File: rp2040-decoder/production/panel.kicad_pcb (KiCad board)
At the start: 4 copper layers, 70 x 70 mm, 511 parts, among them J4 5050662422, Q1 TPM2008, Q2 TPM2008, Q3 TPM2008, Q5 TPM2008, Q6 TPM2008, SW1 BOOT, U1 W25Q16JVUXIQ, U2 MT2492, U3 RP2040, U4 MD9927, U5 MAX98357A, Y1 X252012MMB4SI

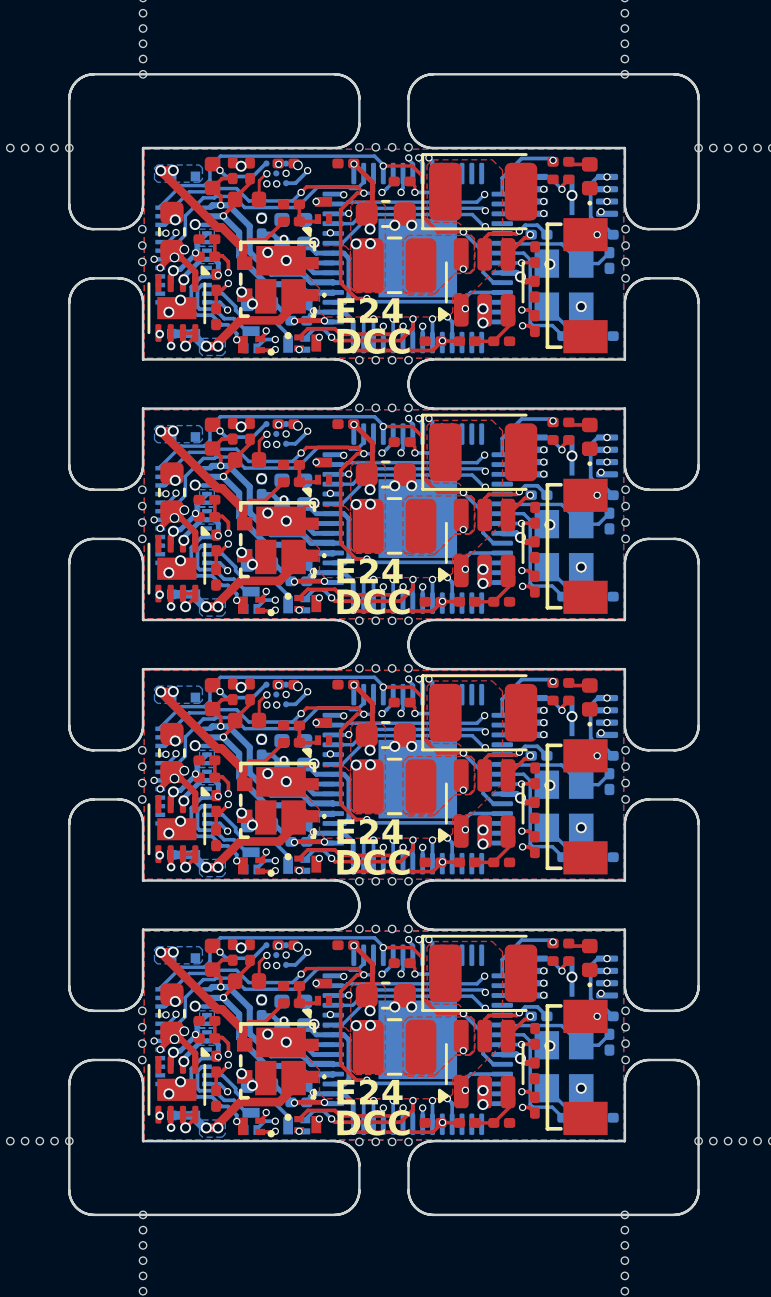
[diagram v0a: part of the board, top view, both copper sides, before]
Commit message: feat: upgrade flash to 8MB
feat: reorganize layout to be cleaner
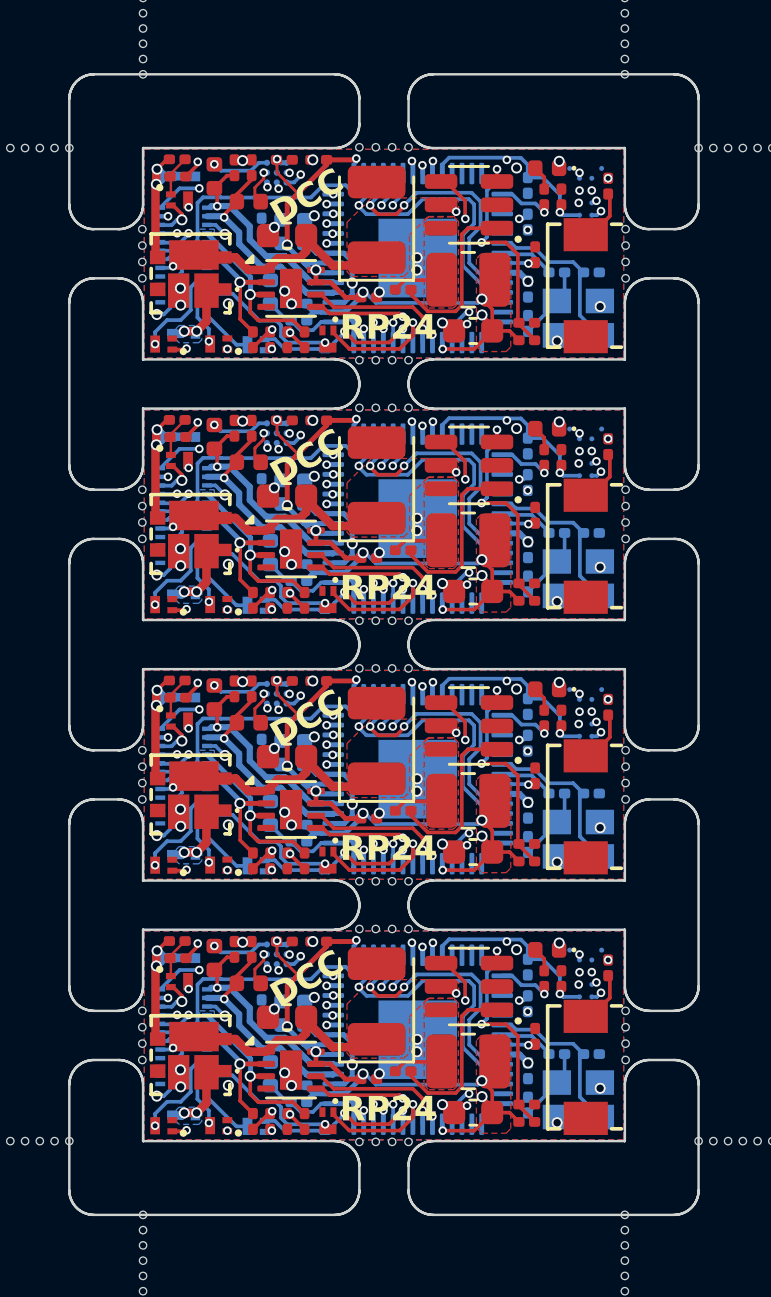
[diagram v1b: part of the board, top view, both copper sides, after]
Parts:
- removed the C1 at (157.7, 50.0)
- removed the C1 at (157.7, 60.6)
- removed the C1 at (157.7, 71.2)
- removed the C1 at (157.7, 39.4)
- removed the C14 at (143.4, 51.7)
- removed the C14 at (143.4, 72.9)
- removed the C14 at (143.4, 62.3)
- removed the C14 at (143.4, 41.1)
- removed the C16 at (146.9, 35.4)
- removed the C16 at (146.9, 46.0)
- removed the C16 at (146.9, 67.2)
- removed the C16 at (146.9, 56.6)
- removed the C17 at (149.2, 57.4)
- removed the C17 at (149.2, 36.2)
- removed the C17 at (149.2, 68.0)
- removed the C17 at (149.2, 46.8)
- removed the C18 at (139.9, 59.4)
- removed the C18 at (139.9, 70.0)
- removed the C18 at (139.9, 38.2)
- removed the C18 at (139.9, 48.8)
- removed the C19 at (150.5, 74.5)
- removed the C19 at (150.5, 53.3)
- removed the C19 at (150.5, 63.9)
- removed the C19 at (150.5, 42.7)
- removed the C2 at (155.7, 57.3)
- removed the C2 at (155.7, 36.1)
- removed the C2 at (155.7, 67.9)
- removed the C2 at (155.7, 46.7)
- removed the C20 at (143.1, 35.7)
- removed the C20 at (143.1, 46.3)
- removed the C20 at (143.1, 67.5)
- removed the C20 at (143.1, 56.9)
- removed the C21 at (144.5, 67.2)
- removed the C21 at (144.5, 35.4)
- removed the C21 at (144.5, 56.6)
- removed the C21 at (144.5, 46.0)
- removed the C22 at (142.3, 46.3)
- removed the C22 at (142.3, 56.9)
- removed the C22 at (142.3, 35.7)
- removed the C22 at (142.3, 67.5)
- removed the C3 at (157.5, 63.6)
- removed the C3 at (157.5, 42.5)
- removed the C3 at (157.5, 74.2)
- removed the C3 at (157.5, 53.0)
- removed the C4 at (152.5, 68.4)
- removed the C4 at (152.5, 57.8)
- removed the C4 at (152.5, 36.6)
- removed the C4 at (152.5, 47.2)
- removed the C6 at (154.6, 63.1)
- removed the C6 at (154.6, 73.7)
- removed the C6 at (154.6, 52.5)
- removed the C6 at (154.6, 41.9)
- removed the C7 at (154.6, 61.7)
- removed the C7 at (154.6, 72.3)
- removed the C7 at (154.6, 40.5)
- removed the C7 at (154.6, 51.1)
- removed the C9 at (148.6, 69.3)
- removed the C9 at (148.6, 37.5)
- removed the C9 at (148.6, 58.7)
- removed the C9 at (148.6, 48.1)
- removed the D1 at (144.2, 50.7)
- removed the D1 at (144.2, 71.9)
- removed the D1 at (144.2, 61.3)
- removed the D1 at (144.2, 40.1)
- removed the D2 at (156.9, 57.1)
- removed the D2 at (156.9, 35.9)
- removed the D2 at (156.9, 67.7)
- removed the D2 at (156.9, 46.5)
- removed the FB1 at (141.5, 46.5)
- removed the FB1 at (141.5, 35.9)
- removed the FB1 at (141.5, 67.7)
- removed the FB1 at (141.5, 57.1)
- removed the FB2 at (142.9, 58.1)
- removed the FB2 at (142.9, 47.5)
- removed the FB2 at (142.9, 68.7)
- removed the FB2 at (142.9, 36.9)
- removed the L1 at (148.9, 71.4)
- removed the L1 at (148.9, 39.6)
- removed the L1 at (148.9, 60.8)
- removed the L1 at (148.9, 50.2)
- removed the Q1 at (146.0, 37.3)
- removed the Q1 at (146.0, 69.1)
- removed the Q1 at (146.0, 58.5)
- removed the Q1 at (146.0, 47.9)
- removed the Q2 at (144.9, 64.0)
- removed the Q2 at (144.9, 53.4)
- removed the Q2 at (144.9, 42.8)
- removed the Q2 at (144.9, 74.6)
- removed the Q3 at (143.1, 42.8)
- removed the Q3 at (143.1, 74.6)
- removed the Q3 at (143.1, 53.4)
- removed the Q3 at (143.1, 64.0)
- removed the Q5 at (145.4, 42.7)
- removed the Q5 at (145.4, 74.5)
- removed the Q5 at (145.4, 53.3)
- removed the Q5 at (145.4, 63.9)
- removed the Q6 at (143.1, 63.8)
- removed the Q6 at (143.1, 74.4)
- removed the Q6 at (143.1, 53.2)
- removed the Q6 at (143.1, 42.6)
- removed the R1 at (144.7, 48.4)
- removed the R1 at (144.7, 59.0)
- removed the R1 at (144.7, 37.8)
- removed the R1 at (144.7, 69.6)
- removed the R10 at (145.0, 63.0)
- removed the R10 at (145.0, 52.4)
- removed the R10 at (145.0, 73.6)
- removed the R10 at (145.0, 41.8)
- removed the R11 at (141.7, 50.9)
- removed the R11 at (141.7, 72.1)
- removed the R11 at (141.7, 40.3)
- removed the R11 at (141.7, 61.5)
- removed the R12 at (141.7, 62.9)
- removed the R12 at (141.7, 41.7)
- removed the R12 at (141.7, 73.5)
- removed the R12 at (141.7, 52.3)
- removed the R13 at (141.3, 60.4)
- removed the R13 at (141.3, 39.2)
- removed the R13 at (141.3, 71.0)
- removed the R13 at (141.3, 49.8)
- removed the R14 at (141.3, 38.5)
- removed the R14 at (141.3, 49.1)
- removed the R14 at (141.3, 70.3)
- removed the R14 at (141.3, 59.7)
- removed the R2 at (144.7, 47.7)
- removed the R2 at (144.7, 58.3)
- removed the R2 at (144.7, 37.1)
- removed the R2 at (144.7, 68.9)
- removed the R4 at (157.5, 59.5)
- removed the R4 at (157.5, 70.1)
- removed the R4 at (157.5, 38.3)
- removed the R4 at (157.5, 48.9)
- removed the R5 at (154.8, 48.9)
- removed the R5 at (154.8, 38.3)
- removed the R5 at (154.8, 59.5)
- removed the R5 at (154.8, 70.1)
- removed the R6 at (156.1, 74.2)
- removed the R6 at (156.1, 63.6)
- removed the R6 at (156.1, 53.0)
- removed the R6 at (156.1, 42.5)
- removed the R7 at (153.3, 53.3)
- removed the R7 at (153.3, 63.9)
- removed the R7 at (153.3, 42.7)
- removed the R7 at (153.3, 74.5)
- removed the R8 at (151.9, 74.5)
- removed the R8 at (151.9, 42.7)
- removed the R8 at (151.9, 53.3)
- removed the R8 at (151.9, 63.9)
- removed the R9 at (155.7, 46.0)
- removed the R9 at (155.7, 35.4)
- removed the R9 at (155.7, 56.6)
- removed the R9 at (155.7, 67.2)
- removed the SW1 at (156.7, 72.2)
- removed the SW1 at (156.7, 61.6)
- removed the SW1 at (156.7, 51.0)
- removed the SW1 at (156.7, 40.4)
- removed the U1 at (156.2, 57.9)
- removed the U1 at (156.2, 47.3)
- removed the U1 at (156.2, 36.7)
- removed the U1 at (156.2, 68.5)
- removed the U2 at (152.6, 72.1)
- removed the U2 at (152.6, 40.3)
- removed the U2 at (152.6, 50.9)
- removed the U2 at (152.6, 61.5)
- removed the U4 at (140.1, 62.5)
- removed the U4 at (140.1, 51.9)
- removed the U4 at (140.1, 41.3)
- removed the U4 at (140.1, 73.1)
- removed the U5 at (144.1, 57.0)
- removed the U5 at (144.1, 67.6)
- removed the U5 at (144.1, 46.4)
- removed the U5 at (144.1, 35.8)
- removed the Y1 at (155.8, 61.6)
- removed the Y1 at (155.8, 51.0)
- removed the Y1 at (155.8, 72.2)
- removed the Y1 at (155.8, 40.4)
- added C1: 10pF, Capacitor_SMD:C_0201_0603Metric, B.Cu at (156.9, 71.7)
- added C1: 10pF, Capacitor_SMD:C_0201_0603Metric, B.Cu at (156.9, 50.5)
- added C1: 10pF, Capacitor_SMD:C_0201_0603Metric, B.Cu at (156.9, 61.1)
- added C1: 10pF, Capacitor_SMD:C_0201_0603Metric, B.Cu at (156.9, 39.9)
- added C14: 10uF, Capacitor_SMD:C_0402_1005Metric, B.Cu at (143.9, 61.9)
- added C14: 10uF, Capacitor_SMD:C_0402_1005Metric, B.Cu at (143.9, 51.3)
- added C14: 10uF, Capacitor_SMD:C_0402_1005Metric, B.Cu at (143.9, 72.5)
- added C14: 10uF, Capacitor_SMD:C_0402_1005Metric, B.Cu at (143.9, 40.7)
- added C16: 100nF, Capacitor_SMD:C_0201_0603Metric, F.Cu at (145.8, 35.3)
- added C16: 100nF, Capacitor_SMD:C_0201_0603Metric, F.Cu at (145.8, 67.1)
- added C16: 100nF, Capacitor_SMD:C_0201_0603Metric, F.Cu at (145.8, 45.9)
- added C16: 100nF, Capacitor_SMD:C_0201_0603Metric, F.Cu at (145.8, 56.5)
- added C17: 100nF, Capacitor_SMD:C_0201_0603Metric, B.Cu at (154.3, 68.1)
- added C17: 100nF, Capacitor_SMD:C_0201_0603Metric, B.Cu at (154.3, 57.5)
- added C17: 100nF, Capacitor_SMD:C_0201_0603Metric, B.Cu at (154.3, 36.3)
- added C17: 100nF, Capacitor_SMD:C_0201_0603Metric, B.Cu at (154.3, 46.9)
- added C18: 10uF, Capacitor_SMD:C_0603_1608Metric, F.Cu at (144.6, 70.2)
- added C18: 10uF, Capacitor_SMD:C_0603_1608Metric, F.Cu at (144.6, 38.4)
- added C18: 10uF, Capacitor_SMD:C_0603_1608Metric, F.Cu at (144.6, 59.6)
- added C18: 10uF, Capacitor_SMD:C_0603_1608Metric, F.Cu at (144.6, 49.0)
- added C19: 100nF, Capacitor_SMD:C_0201_0603Metric, F.Cu at (147.9, 40.9)
- added C19: 100nF, Capacitor_SMD:C_0201_0603Metric, F.Cu at (147.9, 72.7)
- added C19: 100nF, Capacitor_SMD:C_0201_0603Metric, F.Cu at (147.9, 51.5)
- added C19: 100nF, Capacitor_SMD:C_0201_0603Metric, F.Cu at (147.9, 62.1)
- added C2: 100nF, Capacitor_SMD:C_0201_0603Metric, F.Cu at (155.7, 47.4)
- added C2: 100nF, Capacitor_SMD:C_0201_0603Metric, F.Cu at (155.7, 68.6)
- added C2: 100nF, Capacitor_SMD:C_0201_0603Metric, F.Cu at (155.7, 36.8)
- added C2: 100nF, Capacitor_SMD:C_0201_0603Metric, F.Cu at (155.7, 58.0)
- added C20: 220pF, Capacitor_SMD:C_0201_0603Metric, F.Cu at (143.1, 35.6)
- added C20: 220pF, Capacitor_SMD:C_0201_0603Metric, F.Cu at (143.1, 56.8)
- added C20: 220pF, Capacitor_SMD:C_0201_0603Metric, F.Cu at (143.1, 46.2)
- added C20: 220pF, Capacitor_SMD:C_0201_0603Metric, F.Cu at (143.1, 67.4)
- added C21: 100nF, Capacitor_SMD:C_0201_0603Metric, F.Cu at (144.4, 45.9)
- added C21: 100nF, Capacitor_SMD:C_0201_0603Metric, F.Cu at (144.4, 67.1)
- added C21: 100nF, Capacitor_SMD:C_0201_0603Metric, F.Cu at (144.4, 56.5)
- added C21: 100nF, Capacitor_SMD:C_0201_0603Metric, F.Cu at (144.4, 35.3)
- added C22: 220pF, Capacitor_SMD:C_0201_0603Metric, F.Cu at (142.4, 67.4)
- added C22: 220pF, Capacitor_SMD:C_0201_0603Metric, F.Cu at (142.4, 56.8)
- added C22: 220pF, Capacitor_SMD:C_0201_0603Metric, F.Cu at (142.4, 35.6)
- added C22: 220pF, Capacitor_SMD:C_0201_0603Metric, F.Cu at (142.4, 46.2)
- added C3: 10pF, Capacitor_SMD:C_0201_0603Metric, B.Cu at (154.4, 73.7)
- added C3: 10pF, Capacitor_SMD:C_0201_0603Metric, B.Cu at (154.4, 41.9)
- added C3: 10pF, Capacitor_SMD:C_0201_0603Metric, B.Cu at (154.4, 63.1)
- added C3: 10pF, Capacitor_SMD:C_0201_0603Metric, B.Cu at (154.4, 52.5)
- added C4: 22uF, Capacitor_Tantalum_SMD:CP_EIA-3528-21_Kemet-B, F.Cu at (148.2, 69.5)
- added C4: 22uF, Capacitor_Tantalum_SMD:CP_EIA-3528-21_Kemet-B, F.Cu at (148.2, 37.7)
- added C4: 22uF, Capacitor_Tantalum_SMD:CP_EIA-3528-21_Kemet-B, F.Cu at (148.2, 48.3)
- added C4: 22uF, Capacitor_Tantalum_SMD:CP_EIA-3528-21_Kemet-B, F.Cu at (148.2, 58.9)
- added C6: 22nF, Capacitor_SMD:C_0201_0603Metric, F.Cu at (149.3, 72.4)
- added C6: 22nF, Capacitor_SMD:C_0201_0603Metric, F.Cu at (149.3, 40.6)
- added C6: 22nF, Capacitor_SMD:C_0201_0603Metric, F.Cu at (149.3, 51.2)
- added C6: 22nF, Capacitor_SMD:C_0201_0603Metric, F.Cu at (149.3, 61.8)
- added C7: 100nF, Capacitor_SMD:C_0201_0603Metric, B.Cu at (154.4, 40.5)
- added C7: 100nF, Capacitor_SMD:C_0201_0603Metric, B.Cu at (154.4, 51.1)
- added C7: 100nF, Capacitor_SMD:C_0201_0603Metric, B.Cu at (154.4, 61.7)
- added C7: 100nF, Capacitor_SMD:C_0201_0603Metric, B.Cu at (154.4, 72.3)
- added C9: 22uF, Capacitor_SMD:C_0603_1608Metric, F.Cu at (152.1, 42.2)
- added C9: 22uF, Capacitor_SMD:C_0603_1608Metric, F.Cu at (152.1, 52.8)
- added C9: 22uF, Capacitor_SMD:C_0603_1608Metric, F.Cu at (152.1, 74.0)
- added C9: 22uF, Capacitor_SMD:C_0603_1608Metric, F.Cu at (152.1, 63.4)
- added D1: NSR1030QMU, Local Library:NSR1030QMU, F.Cu at (140.6, 50.5)
- added D1: NSR1030QMU, Local Library:NSR1030QMU, F.Cu at (140.6, 71.7)
- added D1: NSR1030QMU, Local Library:NSR1030QMU, F.Cu at (140.6, 39.9)
- added D1: NSR1030QMU, Local Library:NSR1030QMU, F.Cu at (140.6, 61.1)
- added D2: Blue LED, LED_SMD:LED_0402_1005Metric, F.Cu at (155.1, 56.8)
- added D2: Blue LED, LED_SMD:LED_0402_1005Metric, F.Cu at (155.1, 46.2)
- added D2: Blue LED, LED_SMD:LED_0402_1005Metric, F.Cu at (155.1, 67.4)
- added D2: Blue LED, LED_SMD:LED_0402_1005Metric, F.Cu at (155.1, 35.6)
- added FB1: FB_P, Inductor_SMD:L_0402_1005Metric, F.Cu at (141.6, 36.0)
- added FB1: FB_P, Inductor_SMD:L_0402_1005Metric, F.Cu at (141.6, 57.1)
- added FB1: FB_P, Inductor_SMD:L_0402_1005Metric, F.Cu at (141.6, 67.8)
- added FB1: FB_P, Inductor_SMD:L_0402_1005Metric, F.Cu at (141.6, 46.5)
- added FB2: FB_N, Inductor_SMD:L_0402_1005Metric, F.Cu at (143.0, 68.8)
- added FB2: FB_N, Inductor_SMD:L_0402_1005Metric, F.Cu at (143.0, 58.2)
- added FB2: FB_N, Inductor_SMD:L_0402_1005Metric, F.Cu at (143.0, 37.0)
- added FB2: FB_N, Inductor_SMD:L_0402_1005Metric, F.Cu at (143.0, 47.6)
- added L1: 10uH, Inductor_SMD:L_1008_2520Metric, F.Cu at (151.9, 50.8)
- added L1: 10uH, Inductor_SMD:L_1008_2520Metric, F.Cu at (151.9, 40.2)
- added L1: 10uH, Inductor_SMD:L_1008_2520Metric, F.Cu at (151.9, 72.0)
- added L1: 10uH, Inductor_SMD:L_1008_2520Metric, F.Cu at (151.9, 61.4)
- added Q1: TPM2008, Local Library:Diodes_DFN1006-3, F.Cu at (140.2, 47.5)
- added Q1: TPM2008, Local Library:Diodes_DFN1006-3, F.Cu at (140.2, 58.1)
- added Q1: TPM2008, Local Library:Diodes_DFN1006-3, F.Cu at (140.2, 68.7)
- added Q1: TPM2008, Local Library:Diodes_DFN1006-3, F.Cu at (140.2, 36.9)
- added Q2: TPM2008, Local Library:Diodes_DFN1006-3, F.Cu at (146.2, 74.4)
- added Q2: TPM2008, Local Library:Diodes_DFN1006-3, F.Cu at (146.2, 42.6)
- added Q2: TPM2008, Local Library:Diodes_DFN1006-3, F.Cu at (146.2, 53.2)
- added Q2: TPM2008, Local Library:Diodes_DFN1006-3, F.Cu at (146.2, 63.8)
- added Q3: TPM2008, Local Library:Diodes_DFN1006-3, F.Cu at (139.5, 74.6)
- added Q3: TPM2008, Local Library:Diodes_DFN1006-3, F.Cu at (139.5, 42.8)
- added Q3: TPM2008, Local Library:Diodes_DFN1006-3, F.Cu at (139.5, 64.0)
- added Q3: TPM2008, Local Library:Diodes_DFN1006-3, F.Cu at (139.5, 53.4)
- added Q5: TPM2008, Local Library:Diodes_DFN1006-3, B.Cu at (143.3, 53.4)
- added Q5: TPM2008, Local Library:Diodes_DFN1006-3, B.Cu at (143.3, 74.6)
- added Q5: TPM2008, Local Library:Diodes_DFN1006-3, B.Cu at (143.3, 42.8)
- added Q5: TPM2008, Local Library:Diodes_DFN1006-3, B.Cu at (143.3, 64.0)
- added Q6: TPM2008, Local Library:Diodes_DFN1006-3, F.Cu at (141.8, 53.4)
- added Q6: TPM2008, Local Library:Diodes_DFN1006-3, F.Cu at (141.8, 74.6)
- added Q6: TPM2008, Local Library:Diodes_DFN1006-3, F.Cu at (141.8, 64.0)
- added Q6: TPM2008, Local Library:Diodes_DFN1006-3, F.Cu at (141.8, 42.8)
- added R1: 6.8k, Resistor_SMD:R_0201_0603Metric, F.Cu at (140.1, 45.9)
- added R1: 6.8k, Resistor_SMD:R_0201_0603Metric, F.Cu at (140.1, 67.1)
- added R1: 6.8k, Resistor_SMD:R_0201_0603Metric, F.Cu at (140.1, 56.5)
- added R1: 6.8k, Resistor_SMD:R_0201_0603Metric, F.Cu at (140.1, 35.3)
- added R10: 200R, Resistor_SMD:R_0201_0603Metric, B.Cu at (145.0, 52.4)
- added R10: 200R, Resistor_SMD:R_0201_0603Metric, B.Cu at (145.0, 41.8)
- added R10: 200R, Resistor_SMD:R_0201_0603Metric, B.Cu at (145.0, 63.0)
- added R10: 200R, Resistor_SMD:R_0201_0603Metric, B.Cu at (145.0, 73.6)
- added R11: 6.8k, Resistor_SMD:R_0201_0603Metric, F.Cu at (143.2, 42.6)
- added R11: 6.8k, Resistor_SMD:R_0201_0603Metric, F.Cu at (143.2, 53.2)
- added R11: 6.8k, Resistor_SMD:R_0201_0603Metric, F.Cu at (143.2, 74.4)
- added R11: 6.8k, Resistor_SMD:R_0201_0603Metric, F.Cu at (143.2, 63.8)
- added R12: 1k, Resistor_SMD:R_0201_0603Metric, F.Cu at (143.9, 53.2)
- added R12: 1k, Resistor_SMD:R_0201_0603Metric, F.Cu at (143.9, 42.6)
- added R12: 1k, Resistor_SMD:R_0201_0603Metric, F.Cu at (143.9, 74.4)
- added R12: 1k, Resistor_SMD:R_0201_0603Metric, F.Cu at (143.9, 63.8)
- added R13: 6.8k, Resistor_SMD:R_0201_0603Metric, F.Cu at (145.3, 53.2)
- added R13: 6.8k, Resistor_SMD:R_0201_0603Metric, F.Cu at (145.3, 74.4)
- added R13: 6.8k, Resistor_SMD:R_0201_0603Metric, F.Cu at (145.3, 42.6)
- added R13: 6.8k, Resistor_SMD:R_0201_0603Metric, F.Cu at (145.3, 63.8)
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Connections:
- U3 pad 51: Board_2-Net-(U1-IO3) -> Board_2-Net-(U1-IO2)
- U3 pad 52: Board_2-Net-(U1-CLK) -> Board_2-Net-(U1-IO3)
- U3 pad 53: Board_2-Net-(U1-DI(IO0)) -> Board_2-Net-(U1-CLK)
- U3 pad 54: Board_2-Net-(U1-IO2) -> Board_2-Net-(U1-DO(IO1))
- U3 pad 55: Board_2-Net-(U1-DO(IO1)) -> Board_2-Net-(U1-DI(IO0))
- U3 pad 51: Board_3-Net-(U1-IO3) -> Board_3-Net-(U1-IO2)
- U3 pad 52: Board_3-Net-(U1-CLK) -> Board_3-Net-(U1-IO3)
- U3 pad 53: Board_3-Net-(U1-DI(IO0)) -> Board_3-Net-(U1-CLK)
- U3 pad 54: Board_3-Net-(U1-IO2) -> Board_3-Net-(U1-DO(IO1))
- U3 pad 55: Board_3-Net-(U1-DO(IO1)) -> Board_3-Net-(U1-DI(IO0))
- U3 pad 51: Board_1-Net-(U1-IO3) -> Board_1-Net-(U1-IO2)
- U3 pad 52: Board_1-Net-(U1-CLK) -> Board_1-Net-(U1-IO3)
- U3 pad 53: Board_1-Net-(U1-DI(IO0)) -> Board_1-Net-(U1-CLK)
- U3 pad 54: Board_1-Net-(U1-IO2) -> Board_1-Net-(U1-DO(IO1))
- U3 pad 55: Board_1-Net-(U1-DO(IO1)) -> Board_1-Net-(U1-DI(IO0))
- U3 pad 51: Board_0-Net-(U1-IO3) -> Board_0-Net-(U1-IO2)
- U3 pad 52: Board_0-Net-(U1-CLK) -> Board_0-Net-(U1-IO3)
- U3 pad 53: Board_0-Net-(U1-DI(IO0)) -> Board_0-Net-(U1-CLK)
- U3 pad 54: Board_0-Net-(U1-IO2) -> Board_0-Net-(U1-DO(IO1))
- U3 pad 55: Board_0-Net-(U1-DO(IO1)) -> Board_0-Net-(U1-DI(IO0))
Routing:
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- removed copper zone on B.Cu, net Board_0-/TRACK_LEFT
- removed copper zone on In2.Cu, net Board_0-VDC
- removed copper zone on B.Cu, net Board_1-/TRACK_LEFT
- removed copper zone on In2.Cu, net Board_1-VDC
- removed copper zone on B.Cu, net Board_2-/TRACK_LEFT
- removed copper zone on In2.Cu, net Board_2-VDC
- removed copper zone on B.Cu, net Board_3-/TRACK_LEFT
- removed copper zone on In2.Cu, net Board_3-VDC
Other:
- board text added: "RP24"
- board text removed: "E24"

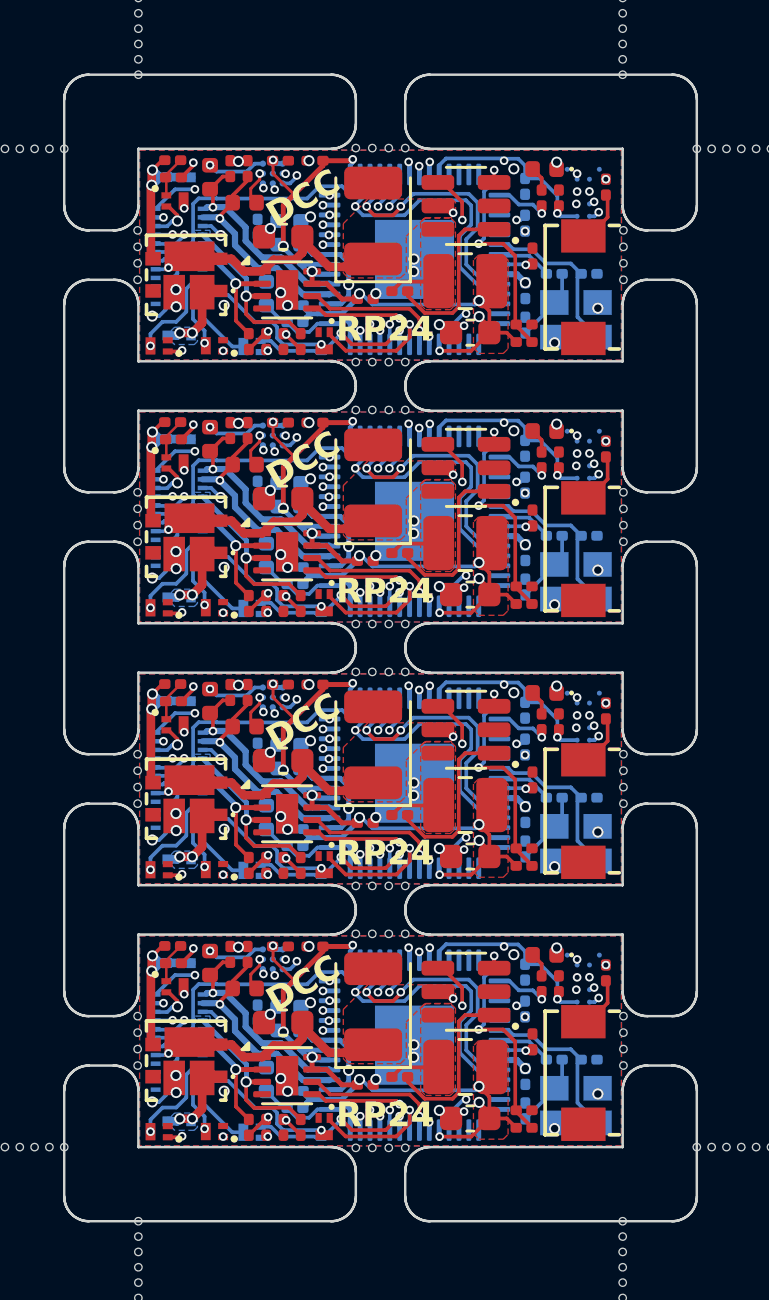
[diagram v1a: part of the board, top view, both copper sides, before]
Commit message: feat: add external capacitor support
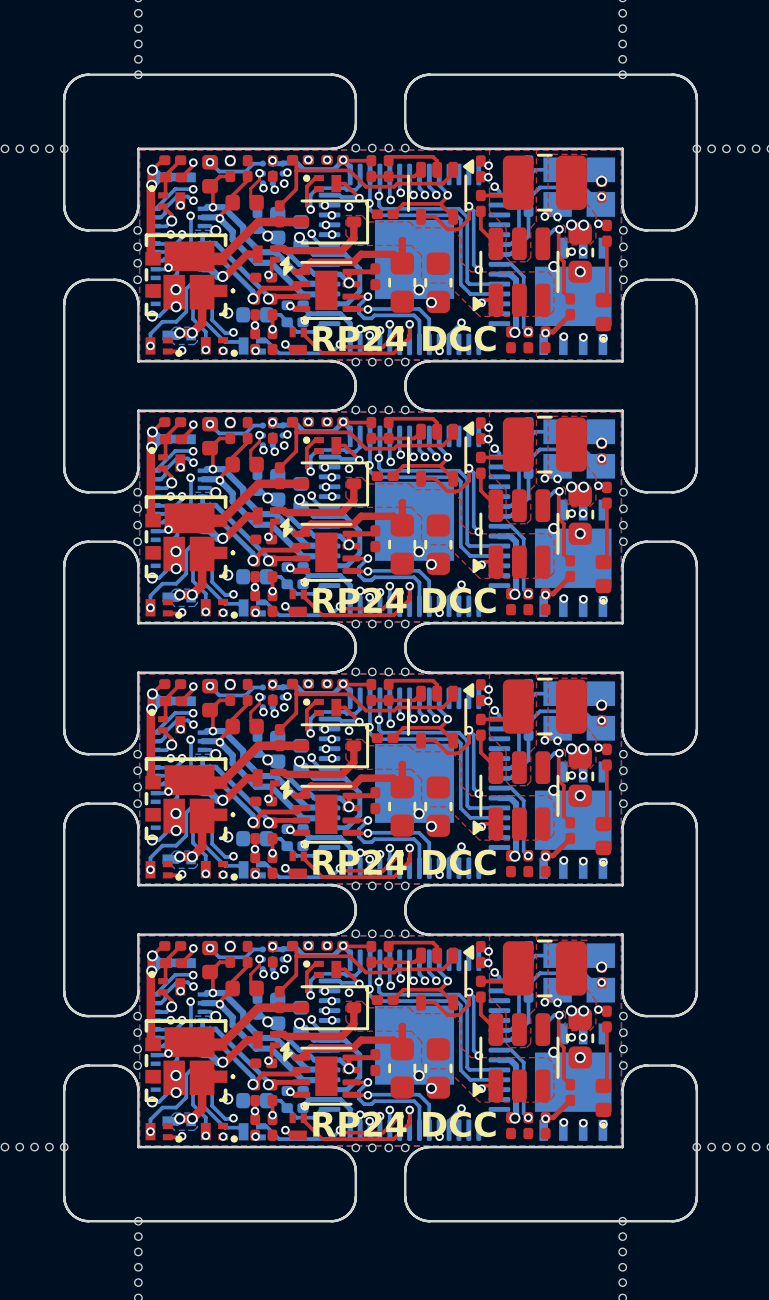
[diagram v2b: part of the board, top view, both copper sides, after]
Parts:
- removed the C1 at (156.9, 71.7)
- removed the C1 at (156.9, 50.5)
- removed the C1 at (156.9, 61.1)
- removed the C1 at (156.9, 39.9)
- removed the C10 at (144.3, 59.4)
- removed the C10 at (144.3, 38.2)
- removed the C10 at (144.3, 70.0)
- removed the C10 at (144.3, 48.8)
- removed the C12 at (143.5, 69.8)
- removed the C12 at (143.5, 59.2)
- removed the C12 at (143.5, 38.0)
- removed the C12 at (143.5, 48.6)
- removed the C13 at (154.7, 49.7)
- removed the C13 at (154.7, 39.1)
- removed the C13 at (154.7, 70.9)
- removed the C13 at (154.7, 60.3)
- removed the C14 at (143.9, 61.9)
- removed the C14 at (143.9, 51.3)
- removed the C14 at (143.9, 72.5)
- removed the C14 at (143.9, 40.7)
- removed the C16 at (145.8, 35.3)
- removed the C16 at (145.8, 67.1)
- removed the C16 at (145.8, 45.9)
- removed the C16 at (145.8, 56.5)
- removed the C17 at (154.3, 68.1)
- removed the C17 at (154.3, 57.5)
- removed the C17 at (154.3, 36.3)
- removed the C17 at (154.3, 46.9)
- removed the C18 at (144.6, 70.2)
- removed the C18 at (144.6, 38.4)
- removed the C18 at (144.6, 59.6)
- removed the C18 at (144.6, 49.0)
- removed the C19 at (147.9, 40.9)
- removed the C19 at (147.9, 72.7)
- removed the C19 at (147.9, 51.5)
- removed the C19 at (147.9, 62.1)
- removed the C2 at (155.7, 47.4)
- removed the C2 at (155.7, 68.6)
- removed the C2 at (155.7, 36.8)
- removed the C2 at (155.7, 58.0)
- removed the C21 at (144.4, 45.9)
- removed the C21 at (144.4, 67.1)
- removed the C21 at (144.4, 56.5)
- removed the C21 at (144.4, 35.3)
- removed the C3 at (154.4, 73.7)
- removed the C3 at (154.4, 41.9)
- removed the C3 at (154.4, 63.1)
- removed the C3 at (154.4, 52.5)
- removed the C4 at (148.2, 69.5)
- removed the C4 at (148.2, 37.7)
- removed the C4 at (148.2, 48.3)
- removed the C4 at (148.2, 58.9)
- removed the C6 at (149.3, 72.4)
- removed the C6 at (149.3, 40.6)
- removed the C6 at (149.3, 51.2)
- removed the C6 at (149.3, 61.8)
- removed the C7 at (154.4, 40.5)
- removed the C7 at (154.4, 51.1)
- removed the C7 at (154.4, 61.7)
- removed the C7 at (154.4, 72.3)
- removed the C8 at (145.3, 38.2)
- removed the C8 at (145.3, 59.4)
- removed the C8 at (145.3, 48.8)
- removed the C8 at (145.3, 70.0)
- removed the C9 at (152.1, 42.2)
- removed the C9 at (152.1, 52.8)
- removed the C9 at (152.1, 74.0)
- removed the C9 at (152.1, 63.4)
- removed the D2 at (155.1, 56.8)
- removed the D2 at (155.1, 46.2)
- removed the D2 at (155.1, 67.4)
- removed the D2 at (155.1, 35.6)
- removed the FB1 at (141.6, 36.0)
- removed the FB1 at (141.6, 57.1)
- removed the FB1 at (141.6, 67.8)
- removed the FB1 at (141.6, 46.5)
- removed the L1 at (151.9, 50.8)
- removed the L1 at (151.9, 40.2)
- removed the L1 at (151.9, 72.0)
- removed the L1 at (151.9, 61.4)
- removed the Q1 at (140.2, 47.5)
- removed the Q1 at (140.2, 58.1)
- removed the Q1 at (140.2, 68.7)
- removed the Q1 at (140.2, 36.9)
- removed the Q2 at (146.2, 74.4)
- removed the Q2 at (146.2, 42.6)
- removed the Q2 at (146.2, 53.2)
- removed the Q2 at (146.2, 63.8)
- removed the Q5 at (143.3, 53.4)
- removed the Q5 at (143.3, 74.6)
- removed the Q5 at (143.3, 42.8)
- removed the Q5 at (143.3, 64.0)
- removed the R11 at (143.2, 42.6)
- removed the R11 at (143.2, 53.2)
- removed the R11 at (143.2, 74.4)
- removed the R11 at (143.2, 63.8)
- removed the R12 at (143.9, 53.2)
- removed the R12 at (143.9, 42.6)
- removed the R12 at (143.9, 74.4)
- removed the R12 at (143.9, 63.8)
- removed the R13 at (145.3, 53.2)
- removed the R13 at (145.3, 74.4)
- removed the R13 at (145.3, 42.6)
- removed the R13 at (145.3, 63.8)
- removed the R14 at (144.6, 74.4)
- removed the R14 at (144.6, 42.6)
- removed the R14 at (144.6, 63.8)
- removed the R14 at (144.6, 53.2)
- removed the R4 at (157.6, 36.4)
- removed the R4 at (157.6, 57.5)
- removed the R4 at (157.6, 68.2)
- removed the R4 at (157.6, 47.0)
- removed R5 (x4): 100k, Resistor_SMD:R_0201_0603Metric
- removed the R6 at (155.5, 71.7)
- removed the R6 at (155.5, 39.9)
- removed the R6 at (155.5, 50.5)
- removed the R6 at (155.5, 61.1)
- removed R7 (x4): 22k, Resistor_SMD:R_0201_0603Metric
- removed R8 (x4): 49.9k, Resistor_SMD:R_0201_0603Metric
- removed the R9 at (155.0, 47.4)
- removed the R9 at (155.0, 68.6)
- removed the R9 at (155.0, 36.8)
- removed the R9 at (155.0, 58.0)
- removed SW1 (x4): BOOT, Local Library:Xunpu_TS-1088-AR02016
- removed the U1 at (156.7, 58.0)
- removed the U1 at (156.7, 36.8)
- removed the U1 at (156.7, 47.4)
- removed the U1 at (156.7, 68.6)
- removed the U2 at (152.0, 47.7)
- removed the U2 at (152.0, 58.3)
- removed the U2 at (152.0, 37.1)
- removed the U2 at (152.0, 68.9)
- removed the U4 at (144.7, 51.1)
- removed the U4 at (144.7, 72.3)
- removed the U4 at (144.7, 61.7)
- removed the U4 at (144.7, 40.5)
- removed the Y1 at (156.4, 41.7)
- removed the Y1 at (156.4, 62.9)
- removed the Y1 at (156.4, 73.5)
- removed the Y1 at (156.4, 52.3)
- added C1: 10pF, Capacitor_SMD:C_0201_0603Metric, B.Cu at (154.5, 67.4)
- added C1: 10pF, Capacitor_SMD:C_0201_0603Metric, B.Cu at (154.5, 35.6)
- added C1: 10pF, Capacitor_SMD:C_0201_0603Metric, B.Cu at (154.5, 56.8)
- added C1: 10pF, Capacitor_SMD:C_0201_0603Metric, B.Cu at (154.5, 46.2)
- added C10: 10uF, Capacitor_SMD:C_0402_1005Metric, B.Cu at (144.3, 48.5)
- added C10: 10uF, Capacitor_SMD:C_0402_1005Metric, B.Cu at (144.3, 59.1)
- added C10: 10uF, Capacitor_SMD:C_0402_1005Metric, B.Cu at (144.3, 69.7)
- added C10: 10uF, Capacitor_SMD:C_0402_1005Metric, B.Cu at (144.3, 37.9)
- added C12: 100nF, Capacitor_SMD:C_0201_0603Metric, B.Cu at (143.5, 48.3)
- added C12: 100nF, Capacitor_SMD:C_0201_0603Metric, B.Cu at (143.5, 58.9)
- added C12: 100nF, Capacitor_SMD:C_0201_0603Metric, B.Cu at (143.5, 69.5)
- added C12: 100nF, Capacitor_SMD:C_0201_0603Metric, B.Cu at (143.5, 37.7)
- added C13: 100nF, Capacitor_SMD:C_0201_0603Metric, F.Cu at (154.5, 53.1)
- added C13: 100nF, Capacitor_SMD:C_0201_0603Metric, F.Cu at (154.5, 42.5)
- added C13: 100nF, Capacitor_SMD:C_0201_0603Metric, F.Cu at (154.5, 63.7)
- added C13: 100nF, Capacitor_SMD:C_0201_0603Metric, F.Cu at (154.5, 74.3)
- added C14: 10uF, Capacitor_SMD:C_0402_1005Metric, B.Cu at (143.4, 41.5)
- added C14: 10uF, Capacitor_SMD:C_0402_1005Metric, B.Cu at (143.4, 73.3)
- added C14: 10uF, Capacitor_SMD:C_0402_1005Metric, B.Cu at (143.4, 62.7)
- added C14: 10uF, Capacitor_SMD:C_0402_1005Metric, B.Cu at (143.4, 52.1)
- added C15: 10pF, Capacitor_SMD:C_0201_0603Metric, F.Cu at (143.8, 61.2)
- added C15: 10pF, Capacitor_SMD:C_0201_0603Metric, F.Cu at (143.8, 50.6)
- added C15: 10pF, Capacitor_SMD:C_0201_0603Metric, F.Cu at (143.8, 71.8)
- added C15: 10pF, Capacitor_SMD:C_0201_0603Metric, F.Cu at (143.8, 40.0)
- added C16: 100nF, Capacitor_SMD:C_0201_0603Metric, F.Cu at (146.7, 67.0)
- added C16: 100nF, Capacitor_SMD:C_0201_0603Metric, F.Cu at (146.7, 56.5)
- added C16: 100nF, Capacitor_SMD:C_0201_0603Metric, F.Cu at (146.7, 45.9)
- added C16: 100nF, Capacitor_SMD:C_0201_0603Metric, F.Cu at (146.7, 35.2)
- added C17: 100nF, Capacitor_SMD:C_0201_0603Metric, F.Cu at (152.6, 35.6)
- added C17: 100nF, Capacitor_SMD:C_0201_0603Metric, F.Cu at (152.6, 67.4)
- added C17: 100nF, Capacitor_SMD:C_0201_0603Metric, F.Cu at (152.6, 56.8)
- added C17: 100nF, Capacitor_SMD:C_0201_0603Metric, F.Cu at (152.6, 46.2)
- added C18: 10uF, Capacitor_SMD:C_0603_1608Metric, F.Cu at (149.4, 72.0)
- added C18: 10uF, Capacitor_SMD:C_0603_1608Metric, F.Cu at (149.4, 61.4)
- added C18: 10uF, Capacitor_SMD:C_0603_1608Metric, F.Cu at (149.4, 50.8)
- added C18: 10uF, Capacitor_SMD:C_0603_1608Metric, F.Cu at (149.4, 40.2)
- added C19: 100nF, Capacitor_SMD:C_0201_0603Metric, F.Cu at (148.3, 40.0)
- added C19: 100nF, Capacitor_SMD:C_0201_0603Metric, F.Cu at (148.3, 61.2)
- added C19: 100nF, Capacitor_SMD:C_0201_0603Metric, F.Cu at (148.3, 50.6)
- added C19: 100nF, Capacitor_SMD:C_0201_0603Metric, F.Cu at (148.3, 71.8)
- added C2: 100nF, Capacitor_SMD:C_0201_0603Metric, F.Cu at (155.2, 63.7)
- added C2: 100nF, Capacitor_SMD:C_0201_0603Metric, F.Cu at (155.2, 74.3)
- added C2: 100nF, Capacitor_SMD:C_0201_0603Metric, F.Cu at (155.2, 53.1)
- added C2: 100nF, Capacitor_SMD:C_0201_0603Metric, F.Cu at (155.2, 42.5)
- added C21: 100nF, Capacitor_SMD:C_0201_0603Metric, F.Cu at (144.1, 56.8)
- added C21: 100nF, Capacitor_SMD:C_0201_0603Metric, F.Cu at (144.1, 35.6)
- added C21: 100nF, Capacitor_SMD:C_0201_0603Metric, F.Cu at (144.1, 46.2)
- added C21: 100nF, Capacitor_SMD:C_0201_0603Metric, F.Cu at (144.1, 67.4)
- added C3: 10pF, Capacitor_SMD:C_0201_0603Metric, F.Cu at (157.4, 57.6)
- added C3: 10pF, Capacitor_SMD:C_0201_0603Metric, F.Cu at (157.4, 47.0)
- added C3: 10pF, Capacitor_SMD:C_0201_0603Metric, F.Cu at (157.4, 68.2)
- added C3: 10pF, Capacitor_SMD:C_0201_0603Metric, F.Cu at (157.4, 36.4)
- added C4: 10uF, Capacitor_SMD:C_0603_1608Metric, F.Cu at (150.8, 72.0)
- added C4: 10uF, Capacitor_SMD:C_0603_1608Metric, F.Cu at (150.8, 40.2)
- added C4: 10uF, Capacitor_SMD:C_0603_1608Metric, F.Cu at (150.8, 61.4)
- added C4: 10uF, Capacitor_SMD:C_0603_1608Metric, F.Cu at (150.8, 50.8)
- added C5: 100nF, Capacitor_SMD:C_0201_0603Metric, F.Cu at (148.7, 58.6)
- added C5: 100nF, Capacitor_SMD:C_0201_0603Metric, F.Cu at (148.7, 69.2)
- added C5: 100nF, Capacitor_SMD:C_0201_0603Metric, F.Cu at (148.7, 48.0)
- added C5: 100nF, Capacitor_SMD:C_0201_0603Metric, F.Cu at (148.7, 37.5)
- added C6: 100nF, Capacitor_SMD:C_0201_0603Metric, F.Cu at (152.6, 37.0)
- added C6: 100nF, Capacitor_SMD:C_0201_0603Metric, F.Cu at (152.6, 58.2)
- added C6: 100nF, Capacitor_SMD:C_0201_0603Metric, F.Cu at (152.6, 68.8)
- added C6: 100nF, Capacitor_SMD:C_0201_0603Metric, F.Cu at (152.6, 47.6)
- added C7: 100nF, Capacitor_SMD:C_0201_0603Metric, F.Cu at (153.8, 42.5)
- added C7: 100nF, Capacitor_SMD:C_0201_0603Metric, F.Cu at (153.8, 63.7)
- added C7: 100nF, Capacitor_SMD:C_0201_0603Metric, F.Cu at (153.8, 74.3)
- added C7: 100nF, Capacitor_SMD:C_0201_0603Metric, F.Cu at (153.8, 53.1)
- added C8: 10uF, Capacitor_SMD:C_0402_1005Metric, B.Cu at (145.3, 38.2)
- added C8: 10uF, Capacitor_SMD:C_0402_1005Metric, B.Cu at (145.3, 48.8)
- added C8: 10uF, Capacitor_SMD:C_0402_1005Metric, B.Cu at (145.3, 59.4)
- added C8: 10uF, Capacitor_SMD:C_0402_1005Metric, B.Cu at (145.3, 70.0)
- added C9: 22uF, Capacitor_SMD:C_0603_1608Metric, F.Cu at (156.6, 60.2)
- added C9: 22uF, Capacitor_SMD:C_0603_1608Metric, F.Cu at (156.6, 49.6)
- added C9: 22uF, Capacitor_SMD:C_0603_1608Metric, F.Cu at (156.6, 39.0)
- added C9: 22uF, Capacitor_SMD:C_0603_1608Metric, F.Cu at (156.6, 70.8)
- added D2: Blue LED, LED_SMD:LED_0402_1005Metric, F.Cu at (157.5, 41.4)
- added D2: Blue LED, LED_SMD:LED_0402_1005Metric, F.Cu at (157.5, 52.0)
- added D2: Blue LED, LED_SMD:LED_0402_1005Metric, F.Cu at (157.5, 62.6)
- added D2: Blue LED, LED_SMD:LED_0402_1005Metric, F.Cu at (157.5, 73.2)
- added D4: 1N5819WS, Diode_SMD:D_SOD-323, F.Cu at (146.4, 59.0)
- added D4: 1N5819WS, Diode_SMD:D_SOD-323, F.Cu at (146.4, 69.6)
- added D4: 1N5819WS, Diode_SMD:D_SOD-323, F.Cu at (146.4, 48.4)
- added D4: 1N5819WS, Diode_SMD:D_SOD-323, F.Cu at (146.4, 37.8)
- added FB1: FB_P, Inductor_SMD:L_0402_1005Metric, F.Cu at (141.6, 67.6)
- added FB1: FB_P, Inductor_SMD:L_0402_1005Metric, F.Cu at (141.6, 35.8)
- added FB1: FB_P, Inductor_SMD:L_0402_1005Metric, F.Cu at (141.6, 57.0)
- added FB1: FB_P, Inductor_SMD:L_0402_1005Metric, F.Cu at (141.6, 46.4)
- added L1: 4.7uH, Inductor_SMD:L_1008_2520Metric, F.Cu at (155.2, 46.8)
- added L1: 4.7uH, Inductor_SMD:L_1008_2520Metric, F.Cu at (155.2, 57.4)
- added L1: 4.7uH, Inductor_SMD:L_1008_2520Metric, F.Cu at (155.2, 36.2)
- added L1: 4.7uH, Inductor_SMD:L_1008_2520Metric, F.Cu at (155.2, 68.0)
- added Q1: TPM2008, Local Library:Diodes_DFN1006-3, F.Cu at (140.1, 47.5)
- added Q1: TPM2008, Local Library:Diodes_DFN1006-3, F.Cu at (140.1, 58.1)
- added Q1: TPM2008, Local Library:Diodes_DFN1006-3, F.Cu at (140.1, 68.7)
- added Q1: TPM2008, Local Library:Diodes_DFN1006-3, F.Cu at (140.1, 36.9)
- added Q2: TPM2008, Local Library:Diodes_DFN1006-3, F.Cu at (145.2, 53.2)
- added Q2: TPM2008, Local Library:Diodes_DFN1006-3, F.Cu at (145.2, 42.6)
- added Q2: TPM2008, Local Library:Diodes_DFN1006-3, F.Cu at (145.2, 63.8)
- added Q2: TPM2008, Local Library:Diodes_DFN1006-3, F.Cu at (145.2, 74.4)
- added Q4: TPM2008, Local Library:Diodes_DFN1006-3, F.Cu at (146.4, 68.0)
- added Q4: TPM2008, Local Library:Diodes_DFN1006-3, F.Cu at (146.4, 36.2)
- added Q4: TPM2008, Local Library:Diodes_DFN1006-3, F.Cu at (146.4, 57.4)
- added Q4: TPM2008, Local Library:Diodes_DFN1006-3, F.Cu at (146.4, 46.8)
- added Q5: TPM2008, Local Library:Diodes_DFN1006-3, B.Cu at (143.3, 53.4)
- added Q5: TPM2008, Local Library:Diodes_DFN1006-3, B.Cu at (143.3, 74.6)
- added Q5: TPM2008, Local Library:Diodes_DFN1006-3, B.Cu at (143.3, 42.8)
- added Q5: TPM2008, Local Library:Diodes_DFN1006-3, B.Cu at (143.3, 64.0)
- added Q7: TPM2008, Local Library:Diodes_DFN1006-3, F.Cu at (143.9, 49.7)
- added Q7: TPM2008, Local Library:Diodes_DFN1006-3, F.Cu at (143.9, 39.1)
- added Q7: TPM2008, Local Library:Diodes_DFN1006-3, F.Cu at (143.9, 60.3)
- added Q7: TPM2008, Local Library:Diodes_DFN1006-3, F.Cu at (143.9, 70.9)
- added R11: 6.8K, Resistor_SMD:R_0201_0603Metric, F.Cu at (143.4, 41.2)
- added R11: 6.8K, Resistor_SMD:R_0201_0603Metric, F.Cu at (143.4, 51.8)
- added R11: 6.8K, Resistor_SMD:R_0201_0603Metric, F.Cu at (143.4, 62.4)
- added R11: 6.8K, Resistor_SMD:R_0201_0603Metric, F.Cu at (143.4, 73.0)
- added R12: 1K, Resistor_SMD:R_0201_0603Metric, F.Cu at (143.4, 42.6)
- added R12: 1K, Resistor_SMD:R_0201_0603Metric, F.Cu at (143.4, 74.4)
- added R12: 1K, Resistor_SMD:R_0201_0603Metric, F.Cu at (143.4, 63.8)
- added R12: 1K, Resistor_SMD:R_0201_0603Metric, F.Cu at (143.4, 53.2)
- added R13: 6.8K, Resistor_SMD:R_0201_0603Metric, F.Cu at (144.1, 62.4)
- added R13: 6.8K, Resistor_SMD:R_0201_0603Metric, F.Cu at (144.1, 41.2)
- added R13: 6.8K, Resistor_SMD:R_0201_0603Metric, F.Cu at (144.1, 51.8)
- added R13: 6.8K, Resistor_SMD:R_0201_0603Metric, F.Cu at (144.1, 73.0)
- added R14: 1K, Resistor_SMD:R_0201_0603Metric, F.Cu at (144.1, 63.8)
- added R14: 1K, Resistor_SMD:R_0201_0603Metric, F.Cu at (144.1, 42.6)
- added R14: 1K, Resistor_SMD:R_0201_0603Metric, F.Cu at (144.1, 74.4)
- added R14: 1K, Resistor_SMD:R_0201_0603Metric, F.Cu at (144.1, 53.2)
- added R15: 1K, Resistor_SMD:R_0201_0603Metric, F.Cu at (156.2, 73.0)
- added R15: 1K, Resistor_SMD:R_0201_0603Metric, F.Cu at (156.2, 62.4)
- added R15: 1K, Resistor_SMD:R_0201_0603Metric, F.Cu at (156.2, 51.8)
- added R15: 1K, Resistor_SMD:R_0201_0603Metric, F.Cu at (156.2, 41.2)
- added R16: 20K, Resistor_SMD:R_0201_0603Metric, F.Cu at (148.1, 56.8)
- added R16: 20K, Resistor_SMD:R_0201_0603Metric, F.Cu at (148.1, 46.2)
- added R16: 20K, Resistor_SMD:R_0201_0603Metric, F.Cu at (148.1, 67.4)
- added R16: 20K, Resistor_SMD:R_0201_0603Metric, F.Cu at (148.1, 35.6)
- added R17: 33K, Resistor_SMD:R_0201_0603Metric, F.Cu at (148.8, 35.6)
- added R17: 33K, Resistor_SMD:R_0201_0603Metric, F.Cu at (148.8, 56.8)
- added R17: 33K, Resistor_SMD:R_0201_0603Metric, F.Cu at (148.8, 46.2)
- added R17: 33K, Resistor_SMD:R_0201_0603Metric, F.Cu at (148.8, 67.4)
- added R3: 100K, Resistor_SMD:R_0201_0603Metric, F.Cu at (144.4, 58.6)
- added R3: 100K, Resistor_SMD:R_0201_0603Metric, F.Cu at (144.4, 48.0)
- added R3: 100K, Resistor_SMD:R_0201_0603Metric, F.Cu at (144.4, 37.4)
- added R3: 100K, Resistor_SMD:R_0201_0603Metric, F.Cu at (144.4, 69.2)
- added R4: 33K, Resistor_SMD:R_0201_0603Metric, F.Cu at (145.3, 56.5)
- added R4: 33K, Resistor_SMD:R_0201_0603Metric, F.Cu at (145.3, 45.9)
- added R4: 33K, Resistor_SMD:R_0201_0603Metric, F.Cu at (145.3, 35.2)
- added R4: 33K, Resistor_SMD:R_0201_0603Metric, F.Cu at (145.3, 67.0)
- added R6: 1K, Resistor_SMD:R_0201_0603Metric, B.Cu at (154.5, 58.2)
- added R6: 1K, Resistor_SMD:R_0201_0603Metric, B.Cu at (154.5, 37.0)
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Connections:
- U3 pad 56: Board_1-Net-(U1-~{CS}) -> Board_1-/BOOT
- U3 pad 56: Board_2-Net-(U1-~{CS}) -> Board_2-/BOOT
- U3 pad 56: Board_3-Net-(U1-~{CS}) -> Board_3-/BOOT
- U3 pad 56: Board_0-Net-(U1-~{CS}) -> Board_0-/BOOT
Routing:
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- added copper zone on F.Cu, net Board_0-/CAP_VDC
- added copper zone on F.Cu, net Board_1-/CAP_VDC
- added copper zone on F.Cu, net Board_2-/CAP_VDC
- added copper zone on F.Cu, net Board_3-/CAP_VDC
- removed copper zone on F.Cu, net Board_0-VDC
- removed copper zone on F.Cu, net Board_1-VDC
- removed copper zone on F.Cu, net Board_2-VDC
- removed copper zone on F.Cu, net Board_3-VDC
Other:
- board text added: "RP24 DCC"
- board text removed: "DCC"
- board text removed: "RP24"
